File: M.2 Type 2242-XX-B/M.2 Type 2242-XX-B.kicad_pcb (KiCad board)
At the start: 2 copper layers, 30 x 42 mm, 83 parts, among them J1 ANT1, J2 ANT2, M1 MountingHole_Pad, U1 M.2_NGFF_Socket2_KeyB_SSIC_Ad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, U2 AS193-73, U3 M74VHC1GT04DFT1G, U4 ADF7021BCPZ, U5 STM32F103C8Tx, X1 FT5HNBPK19.44-T1, Y1 12MHz

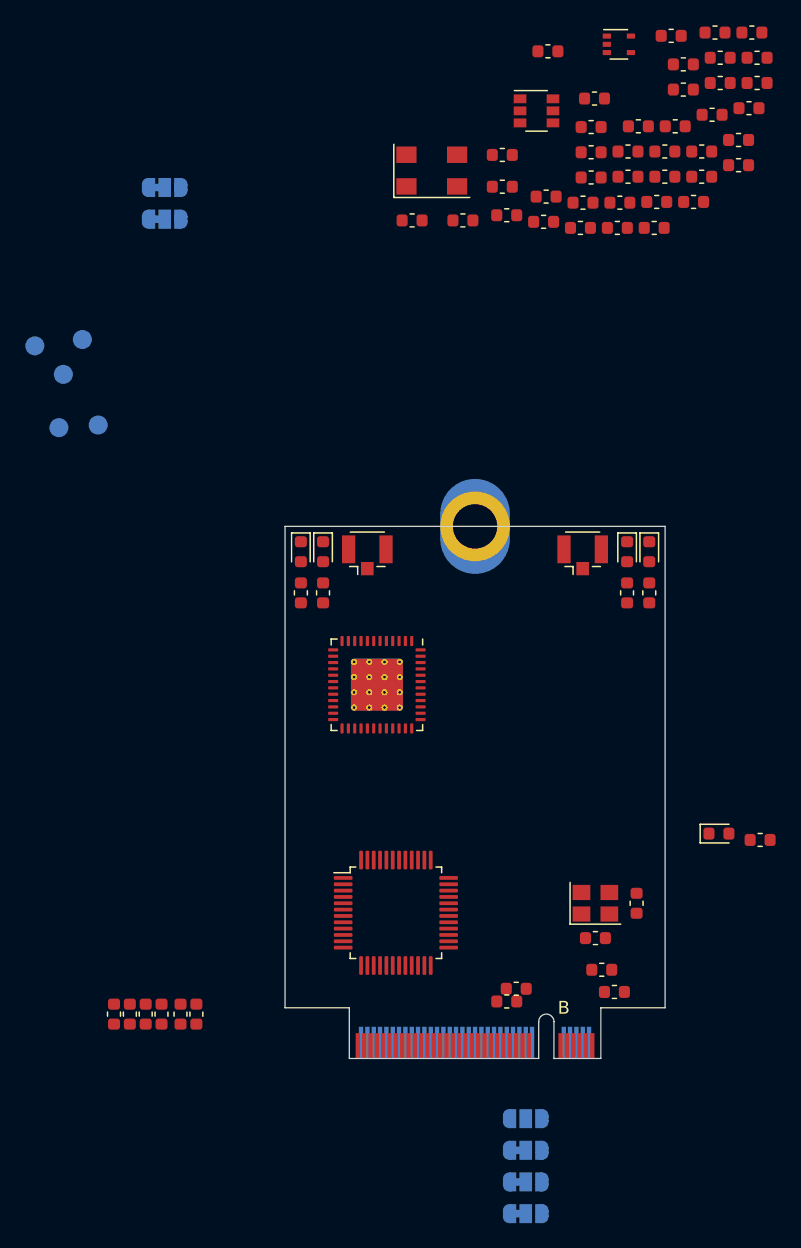
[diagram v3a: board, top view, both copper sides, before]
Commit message: Almost everything placed
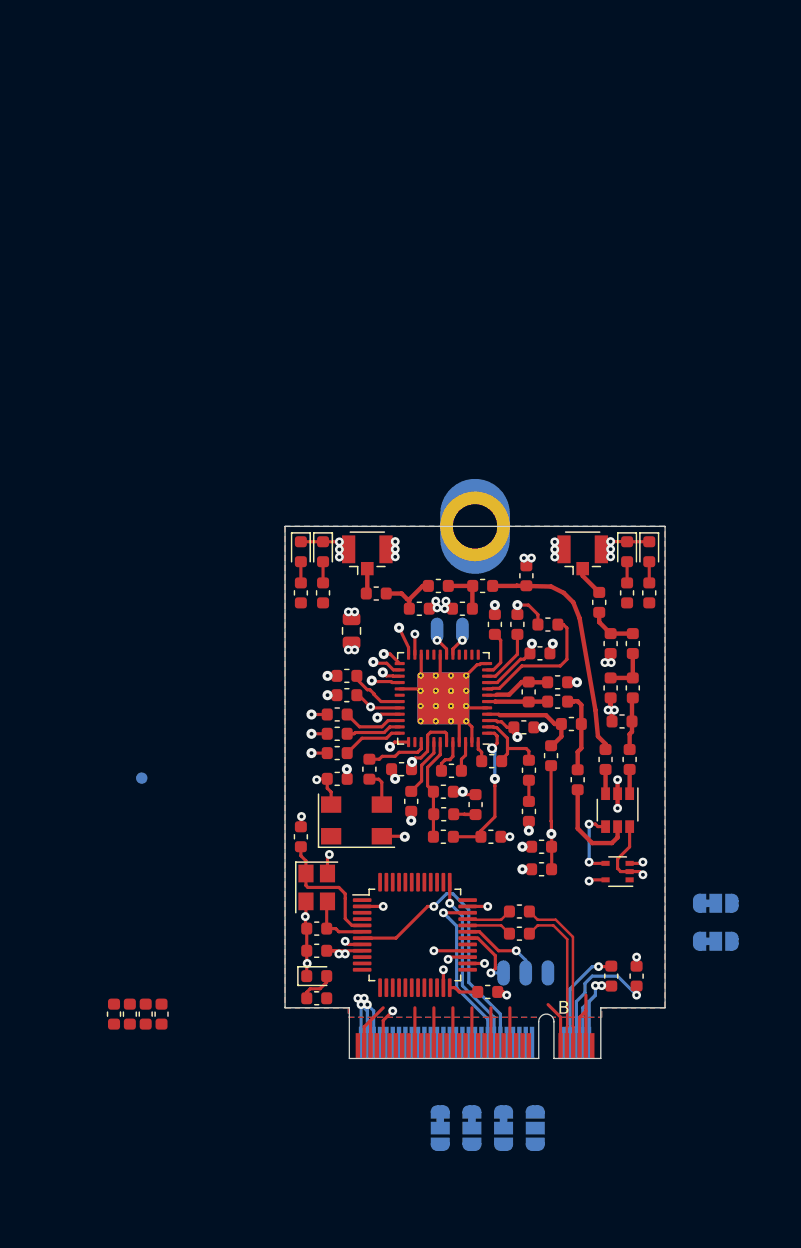
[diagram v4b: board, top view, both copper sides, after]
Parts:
- removed C1: 10uF, Capacitor_SMD:C_0603_1608Metric
- removed C10, C13, C20, C21: 100nF, Capacitor_SMD:C_0603_1608Metric
- removed C11, C12, C19, C22, C23, C6: 10nF, Capacitor_SMD:C_0603_1608Metric
- removed C14: 470pF, Capacitor_SMD:C_0603_1608Metric
- removed C15: 22nF, Capacitor_SMD:C_0603_1608Metric
- removed C16: 15nF, Capacitor_SMD:C_0603_1608Metric
- removed C17: 1nF, Capacitor_SMD:C_0603_1608Metric
- removed C18: 22pF, Capacitor_SMD:C_0603_1608Metric
- removed C34: 6.8pF, Capacitor_SMD:C_0603_1608Metric
- removed C35, C4: C, Capacitor_SMD:C_0603_1608Metric
- removed C36, C7, C9: 11pF, Capacitor_SMD:C_0603_1608Metric
- removed C8: 220pF, Capacitor_SMD:C_0603_1608Metric
- removed L1: 180nH, Inductor_SMD:L_0603_1608Metric
- removed L2: 68nH, Inductor_SMD:L_0603_1608Metric
- removed L3: 17nH, Inductor_SMD:L_0603_1608Metric
- removed L4: 0R, Inductor_SMD:L_0603_1608Metric
- removed L5: 22nH, Inductor_SMD:L_0603_1608Metric
- removed L6: 20nH, Inductor_SMD:L_0603_1608Metric
- removed R1: 1K1, Resistor_SMD:R_0603_1608Metric
- removed R2: 3R9, Resistor_SMD:R_0603_1608Metric
- removed R3: 3K6, Resistor_SMD:R_0603_1608Metric
- removed R4: 560R, Resistor_SMD:R_0603_1608Metric
- removed R5: 270R, Resistor_SMD:R_0603_1608Metric
- removed R6, R7, R8: 1K, Resistor_SMD:R_0603_1608Metric
- removed TP1: FILT_I, TestPoint:TestPoint_Pad_D1.5mm
- removed TP2: ~FILT_I, TestPoint:TestPoint_Pad_D1.5mm
- removed U4: ADF7021BCPZ, Package_CSP:LFCSP-48-1EP_7x7mm_P0.5mm_EP4.1x4.1mm_ThermalVias
- removed X1: FT5HNBPK19.44-T1, aausat:FOX924
- added C401: 10uF, Capacitor_SMD:C_0805_2012Metric, F.Cu at (1.25, 8.25)
- added C404: C, Capacitor_SMD:C_0603_1608Metric, F.Cu at (21.7, 9.25)
- added C405: 6.8pF, Capacitor_SMD:C_0603_1608Metric, F.Cu at (21.7, 12.8)
- added C407: C, Capacitor_SMD:C_0603_1608Metric, F.Cu at (22.6, 15.4)
- added C408: 10nF, Capacitor_SMD:C_0603_1608Metric, F.Cu at (16.2, 27.1)
- added C409: 11pF, Capacitor_SMD:C_0603_1608Metric, F.Cu at (17.5, 13.8)
- added C410: 220pF, Capacitor_SMD:C_0603_1608Metric, F.Cu at (16.2, 25.3)
- added C411: 11pF, Capacitor_SMD:C_0603_1608Metric, F.Cu at (17.5, 12.3)
- added C412: 11pF, Capacitor_SMD:C_0603_1608Metric, F.Cu at (18.6, 15.6)
- added C413: 100nF, Capacitor_SMD:C_0603_1608Metric, F.Cu at (15.2, 22.5)
- added C414: 10nF, Capacitor_SMD:C_0603_1608Metric, F.Cu at (14.8, 15.9)
- added C415: 10nF, Capacitor_SMD:C_0603_1608Metric, F.Cu at (16.1, 10.0)
- added C416: 100nF, Capacitor_SMD:C_0603_1608Metric, F.Cu at (12.6, 7.74)
- added C417: 470pF, Capacitor_SMD:C_0603_1608Metric, F.Cu at (12.2, 24.5)
- added C418: 22nF, Capacitor_SMD:C_0603_1608Metric, F.Cu at (12.3, 18.5)
- added C419: 15nF, Capacitor_SMD:C_0603_1608Metric, F.Cu at (11.0, 22.0)
- added C420: 1nF, Capacitor_SMD:C_0603_1608Metric, F.Cu at (8.50, 20.9)
- added C421: 22pF, Capacitor_SMD:C_0603_1608Metric, F.Cu at (2.66, 19.2)
- added C422: 10nF, Capacitor_SMD:C_0603_1608Metric, F.Cu at (0.12, 19.9)
- added C423: 100nF, Capacitor_SMD:C_0603_1608Metric, F.Cu at (5.96, 21.7)
- added C424: 100nF, Capacitor_SMD:C_0603_1608Metric, F.Cu at (0.88, 11.8)
- added C425: 10nF, Capacitor_SMD:C_0603_1608Metric, F.Cu at (5.20, 19.2)
- added C426: 10nF, Capacitor_SMD:C_0603_1608Metric, F.Cu at (0.88, 13.3)
- added C427: C, Capacitor_SMD:C_0603_1608Metric, F.Cu at (6.60, 6.50)
- added C428: 6.8pF, Capacitor_SMD:C_0603_1608Metric, F.Cu at (10.0, 6.50)
- added C429: C, Capacitor_SMD:C_0603_1608Metric, F.Cu at (15.1, 3.90)
- added L401: 0R, Inductor_SMD:L_0603_1608Metric, F.Cu at (20.8, 6.00)
- added L402: 22nH, Inductor_SMD:L_0603_1608Metric, F.Cu at (23.4, 9.25)
- added L403: 20nH, Inductor_SMD:L_0603_1608Metric, F.Cu at (23.4, 12.8)
- added L404: 180nH, Inductor_SMD:L_0603_1608Metric, F.Cu at (15.2, 13.1)
- added L405: 68nH, Inductor_SMD:L_0603_1608Metric, F.Cu at (17.0, 18.1)
- added L406: 17nH, Inductor_SMD:L_0603_1608Metric, F.Cu at (9.13, 19.3)
- added L407: 0R, Inductor_SMD:L_0603_1608Metric, F.Cu at (3.20, 5.30)
- added L408: 22nH, Inductor_SMD:L_0603_1608Metric, F.Cu at (8.10, 4.70)
- added L409: 20nH, Inductor_SMD:L_0603_1608Metric, F.Cu at (11.6, 4.70)
- added LOGO401: TestPoint_Alt_Short, aausat:KiCad-Logo_Back, B.Cu at (-16.8, 17.7)
- added R401: 1K1, Resistor_SMD:R_0603_1608Metric, F.Cu at (16.8, 7.75)
- added R402: 3R9, Resistor_SMD:R_0603_1608Metric, F.Cu at (15.2, 19.2)
- added R403: 3K6, Resistor_SMD:R_0603_1608Metric, F.Cu at (14.3, 7.74)
- added R404: 560R, Resistor_SMD:R_0603_1608Metric, F.Cu at (8.50, 24.5)
- added R405: 270R, Resistor_SMD:R_0603_1608Metric, F.Cu at (8.53, 22.7)
- added R406: 1K, Resistor_SMD:R_0603_1608Metric, F.Cu at (0.12, 14.8)
- added R407: 1K, Resistor_SMD:R_0603_1608Metric, F.Cu at (0.12, 16.4)
- added R408: 1K, Resistor_SMD:R_0603_1608Metric, F.Cu at (0.12, 17.9)
- added TP401: FILT_I, aausat:TestPad, B.Cu at (10.0, 8.20)
- added TP402: ~FILT_I, aausat:TestPad, B.Cu at (8.00, 8.20)
- added U403: ADF7021BCPZ, Package_CSP:LFCSP-48-1EP_7x7mm_P0.5mm_EP4.1x4.1mm_ThermalVias, F.Cu at (8.50, 13.6)
- added X401: FT5HNBPK19.44-T1, aausat:FOX924, F.Cu at (1.64, 23.2)
- TP201: renamed from TP3; footprint TestPoint:TestPoint_Pad_D1.5mm -> aausat:TestPad
- TP202: renamed from TP4; footprint TestPoint:TestPoint_Pad_D1.5mm -> aausat:TestPad
- TP203: renamed from TP5; footprint TestPoint:TestPoint_Pad_D1.5mm -> aausat:TestPad
- moved SJ202 73.7 mm to (30.0, 32.8)
- moved SJ201 69.3 mm to (30.0, 29.8)
- moved U402 65.3 mm to (22.2, 27.2), turned to 180 degrees
- moved TP202 62.9 mm to (15.0, 35.2), turned to 90 degrees
- moved TP203 60.8 mm to (16.8, 35.2), turned to 90 degrees
- moved TP201 60.0 mm to (13.2, 35.2), turned to 90 degrees
- moved U401 55.6 mm to (22.2, 22.4), turned to 270 degrees
- moved C406 55.1 mm to (19.1, 20.0), turned to 270 degrees
- moved C403 44.0 mm to (21.3, 18.4), turned to 90 degrees
- moved C402 44.0 mm to (23.2, 18.4), turned to 90 degrees
- moved R204 37.2 mm to (-1.50, 37.2), turned to 180 degrees
- moved D202 33.7 mm to (-1.50, 35.5)
- moved C202 25.3 mm to (-1.50, 31.8), turned to 180 degrees
- moved C201 24.6 mm to (-2.75, 24.5), turned to 90 degrees
- moved C208 24.3 mm to (12.0, 36.8), turned to 0 degrees
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- renumbered C24 to C201, C25 to C202, C28 to C203, C29 to C204, C30 to C205, C31 to C206, C32 to C207, C33 to C208, C2 to C402, C3 to C403, C5 to C406, D1 to D201, D2 to D202, D3 to D203, D4 to D204, D5 to D205, J1 to J101, J2 to J102, JP1 to JP301, JP2 to JP302, JP3 to JP303, JP4 to JP304, M1 to M201, R15 to R201, R16 to R202, R17 to R203, R18 to R204, R19 to R205, R20 to R206, R21 to R207, R22 to R301, R23 to R302, SJ1 to SJ201, SJ2 to SJ202, U5 to U201, U1 to U301, U2 to U401, U3 to U402, Y1 to Y201
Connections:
- C402 pad 2: /Radio Tranceiver/ANT_A -> /Radio Tranceiver/RF_B
- C403 pad 2: /Radio Tranceiver/ANT_B -> /Radio Tranceiver/RF_A
- R202 pad 1: /M.2 NGFF Fingers/USB_D- -> /Microcontroller/USB_OTG_FS_D-
- R202 pad 2: /Microcontroller/USB_OTG_FS_D- -> /M.2 NGFF Fingers/USB_D-
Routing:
- net GND: track 0.00 -> 121.5 mm, vias 0 -> 52
- net +3V3: track 0.00 -> 58.6 mm, vias 0 -> 17
- net /Microcontroller/STM_RESET: track 0.00 -> 21.9 mm, vias 0 -> 1
- net /Radio Tranceiver/RF_A: track 0.00 -> 18.9 mm
- net /Microcontroller/SWCLK: track 0.00 -> 14.1 mm, vias 0 -> 1
- net /Microcontroller/SWDIO: track 0.00 -> 13.6 mm, vias 0 -> 1
- net /M.2 NGFF Fingers/USB_D+: track 0.00 -> 12.9 mm
- net /M.2 NGFF Fingers/USB_D-: track 0.00 -> 12.1 mm
- net Net-(C417-Pad1): track 0.00 -> 11.7 mm, vias 0 -> 2
- net Net-(R302-Pad1): track 0.00 -> 10.6 mm, vias 0 -> 1
- net Net-(R401-Pad1): track 0.00 -> 10.6 mm
- net Net-(C201-Pad1): track 0.00 -> 10.4 mm
- net Net-(C412-Pad2): track 0.00 -> 8.32 mm
- net Net-(R301-Pad2): track 0.00 -> 8.24 mm, vias 0 -> 1
- net Net-(C420-Pad1): track 0.00 -> 8.10 mm
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- added copper zone on In1.Cu, net +3V3
- added copper zone on B.Cu, net GND
- added copper zone on F.Cu, net GND
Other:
- copper layers 2 -> 4

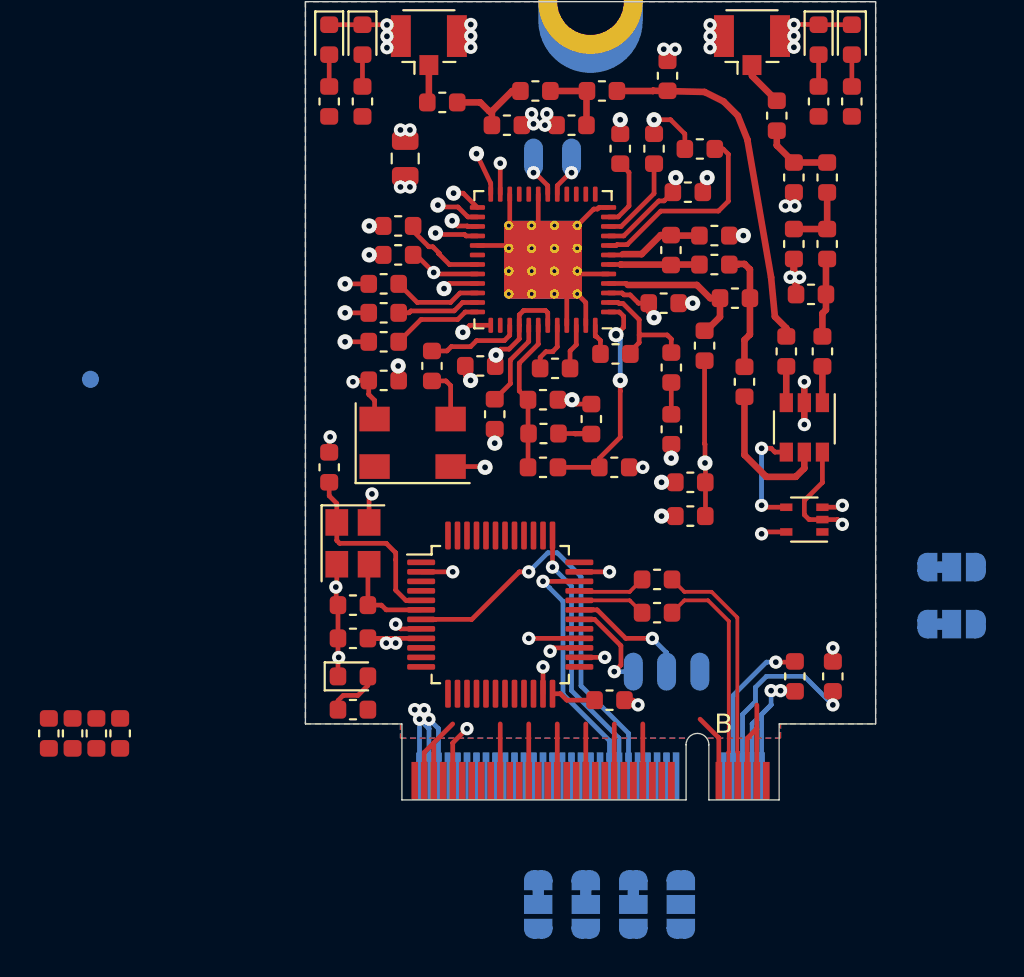
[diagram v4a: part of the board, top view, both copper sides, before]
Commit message: Remove the solder pads for the config pins
Lets hope it is working as is. The board does not really have a lot of
real estate left...
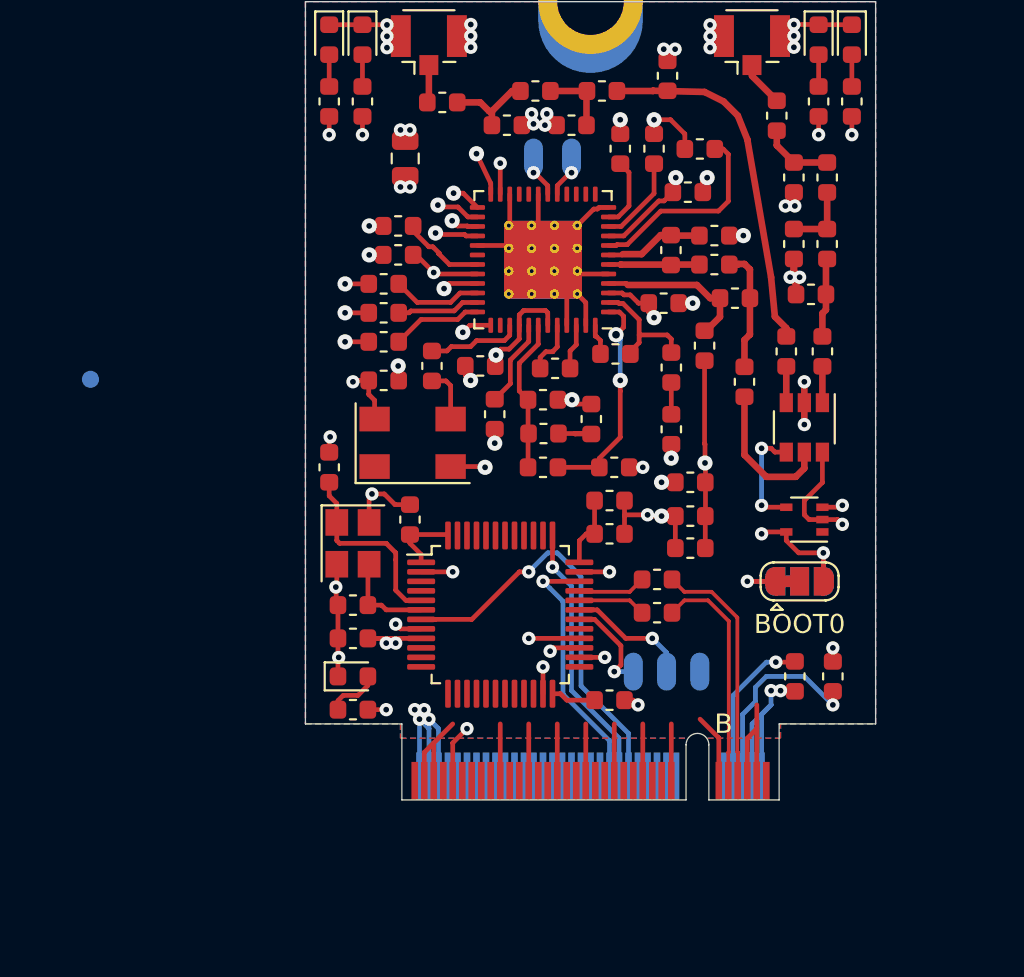
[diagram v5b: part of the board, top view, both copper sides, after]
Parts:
- removed JP301: CONFIG_0, Jumper:SolderJumper-3_P1.3mm_Bridged12_RoundedPad1.0x1.5mm
- removed JP302: CONFIG_1, Jumper:SolderJumper-3_P1.3mm_Bridged12_RoundedPad1.0x1.5mm
- removed JP303: CONFIG_2, Jumper:SolderJumper-3_P1.3mm_Bridged12_RoundedPad1.0x1.5mm
- removed JP304: CONFIG_3, Jumper:SolderJumper-3_P1.3mm_Open_RoundedPad1.0x1.5mm
- SJ201: moved to F.Cu
- moved C205 35.1 mm to (16.2, 28.8), turned to 180 degrees
- moved C203 30.8 mm to (12.0, 26.2), turned to 0 degrees
- moved C206 29.0 mm to (12.0, 28.0), turned to 0 degrees
- moved C204 19.0 mm to (1.50, 27.2), turned to 90 degrees
- moved SJ202 8.31 mm to (22.0, 30.5)
- moved SJ201 8.04 mm to (22.0, 30.5)
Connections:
- U301 pad 21: /M.2 NGFF Fingers/CONFIG_0 -> GND
- U301 pad 69: /M.2 NGFF Fingers/CONFIG_1 -> GND
- U301 pad 75: /M.2 NGFF Fingers/CONFIG_2 -> GND
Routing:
- net +3V3: track 58.6 -> 73.5 mm, vias 17 -> 18
- net GND: track 121.5 -> 135.1 mm, vias 52 -> 54
- net /Microcontroller/LED_B_TX: track 1.34 -> 2.30 mm, vias 1 -> 2
- net /Microcontroller/LED_B_RX: track 1.61 -> 2.57 mm, vias 1 -> 2
- net /Microcontroller/LED_A_TX: track 0.00 -> 0.96 mm, vias 0 -> 1
- net /Microcontroller/LED_A_RX: track 0.00 -> 0.96 mm, vias 0 -> 1
- net /Microcontroller/LED0: track 1.66 -> 2.62 mm, vias 1 -> 2

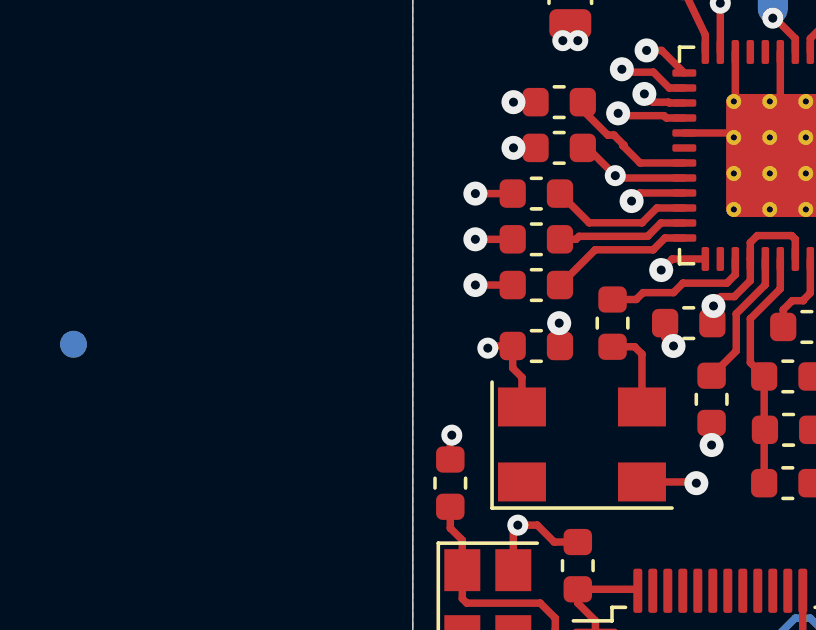
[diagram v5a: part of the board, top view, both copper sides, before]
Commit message: Fix 3D model path for M.2 connector
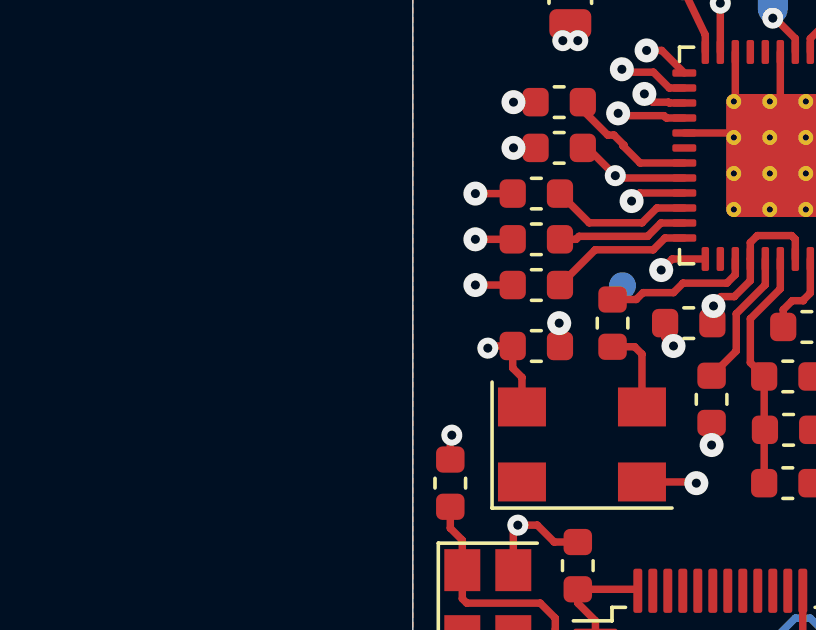
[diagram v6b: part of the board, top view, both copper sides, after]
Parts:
- moved LOGO401 18.4 mm to (1.50, 15.8)

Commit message: Board more or less completely routed
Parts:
- C205: moved to B.Cu
- moved LOGO401 15.0 mm to (16.5, 16.5), turned to 180 degrees
- moved C205 11.6 mm to (7.55, 36.5)
- moved TP201 4.56 mm to (17.8, 34.5), turned to 180 degrees
- moved TP203 4.37 mm to (17.8, 31.0), turned to 180 degrees
- moved TP202 3.72 mm to (17.8, 32.8), turned to 180 degrees
- moved C408 3.40 mm to (17.2, 23.8)
- moved C410 3.26 mm to (16.5, 22.0)
- moved C413 1.90 mm to (13.5, 21.8)
- moved R404 1.50 mm to (10.0, 24.5)
- moved C401 1.06 mm to (2.00, 7.50), turned to 180 degrees
- moved C417 1.00 mm to (13.2, 24.5)
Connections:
- U301 pad 33: GND -> Net-(U301-Pad33)
- U301 pad 39: GND -> Net-(U301-Pad39)
- U301 pad 45: GND -> Net-(U301-Pad45)
- U301 pad 51: GND -> Net-(U301-Pad51)
- U301 pad 57: GND -> Net-(U301-Pad57)
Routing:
- net /Microcontroller/LED_A_RX: track 0.96 -> 50.0 mm, vias 1 -> 4
- net /Microcontroller/LED_A_TX: track 0.96 -> 45.7 mm, vias 1 -> 2
- net /Microcontroller/LED_B_TX: track 2.30 -> 43.6 mm
- net /Microcontroller/LED_B_RX: track 2.57 -> 43.0 mm
- net /Microcontroller/ADF1_SREAD: track 1.46 -> 39.5 mm, vias 1 -> 2
- net /Microcontroller/ADF1_CE: track 2.30 -> 39.1 mm, vias 1 -> 2
- net /Microcontroller/ADF1_TEST_A: track 1.63 -> 38.0 mm, vias 1 -> 4
- net /Microcontroller/ADF1_SLE: track 1.57 -> 35.7 mm, vias 1 -> 2
- net /Microcontroller/ADF1_SDATA: track 2.34 -> 35.2 mm, vias 1 -> 2
- net /Microcontroller/ADF1_SCLK: track 2.27 -> 33.8 mm, vias 1 -> 2
- net /Microcontroller/ADF1_SWD: track 1.87 -> 30.3 mm, vias 1 -> 2
- net /Microcontroller/ADF1_ANT_SELECT: track 5.90 -> 31.8 mm, vias 1 -> 2
- net /Microcontroller/BOOT0: track 0.00 -> 24.7 mm, vias 0 -> 2
- net /Microcontroller/BOOT1: track 0.00 -> 22.9 mm, vias 0 -> 1
- net /Microcontroller/LED1: track 0.00 -> 19.6 mm, vias 0 -> 1
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- added copper zone on VCC, net +3V3
- added copper zone on GND, net GND
- removed copper zone on In1.Cu, net +3V3
- removed copper zone on B.Cu, net GND
- removed copper zone on F.Cu, net GND

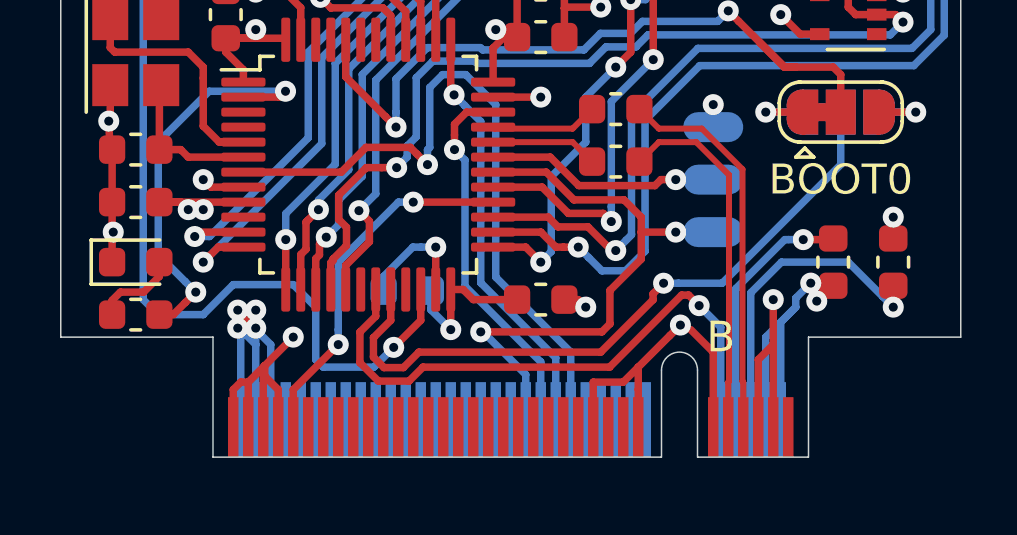
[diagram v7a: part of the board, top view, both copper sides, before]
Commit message: Update clearance rules for M.2 fingers
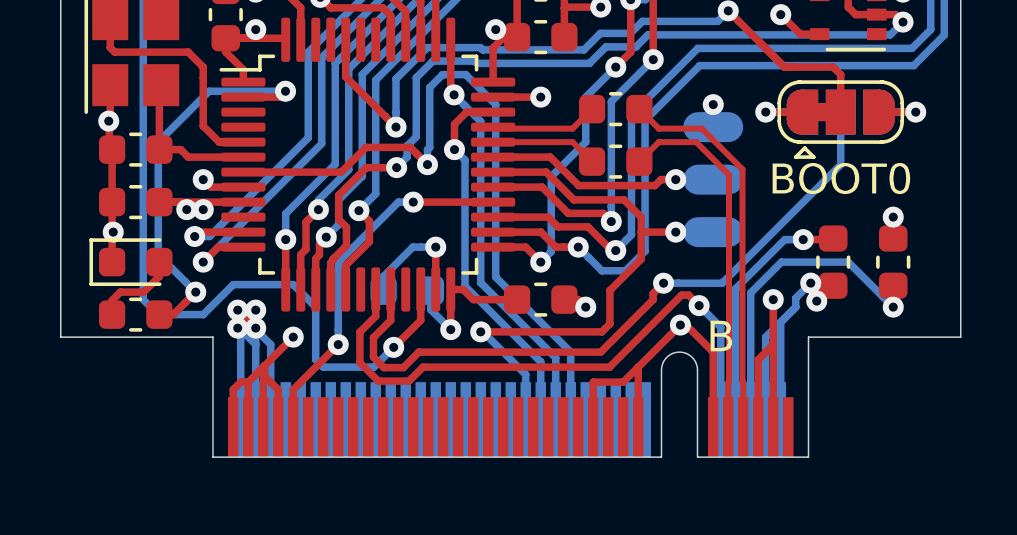
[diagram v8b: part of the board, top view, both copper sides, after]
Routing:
- net +3V3: track 72.3 -> 74.6 mm
